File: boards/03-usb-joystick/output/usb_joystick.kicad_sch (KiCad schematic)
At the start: 19 parts, among them J1 TYPE-C, J2 Joystick, SW1 Button, SW2 Button, SW3 Button, SW4 Button, U1 MCU, Y1 16MHz

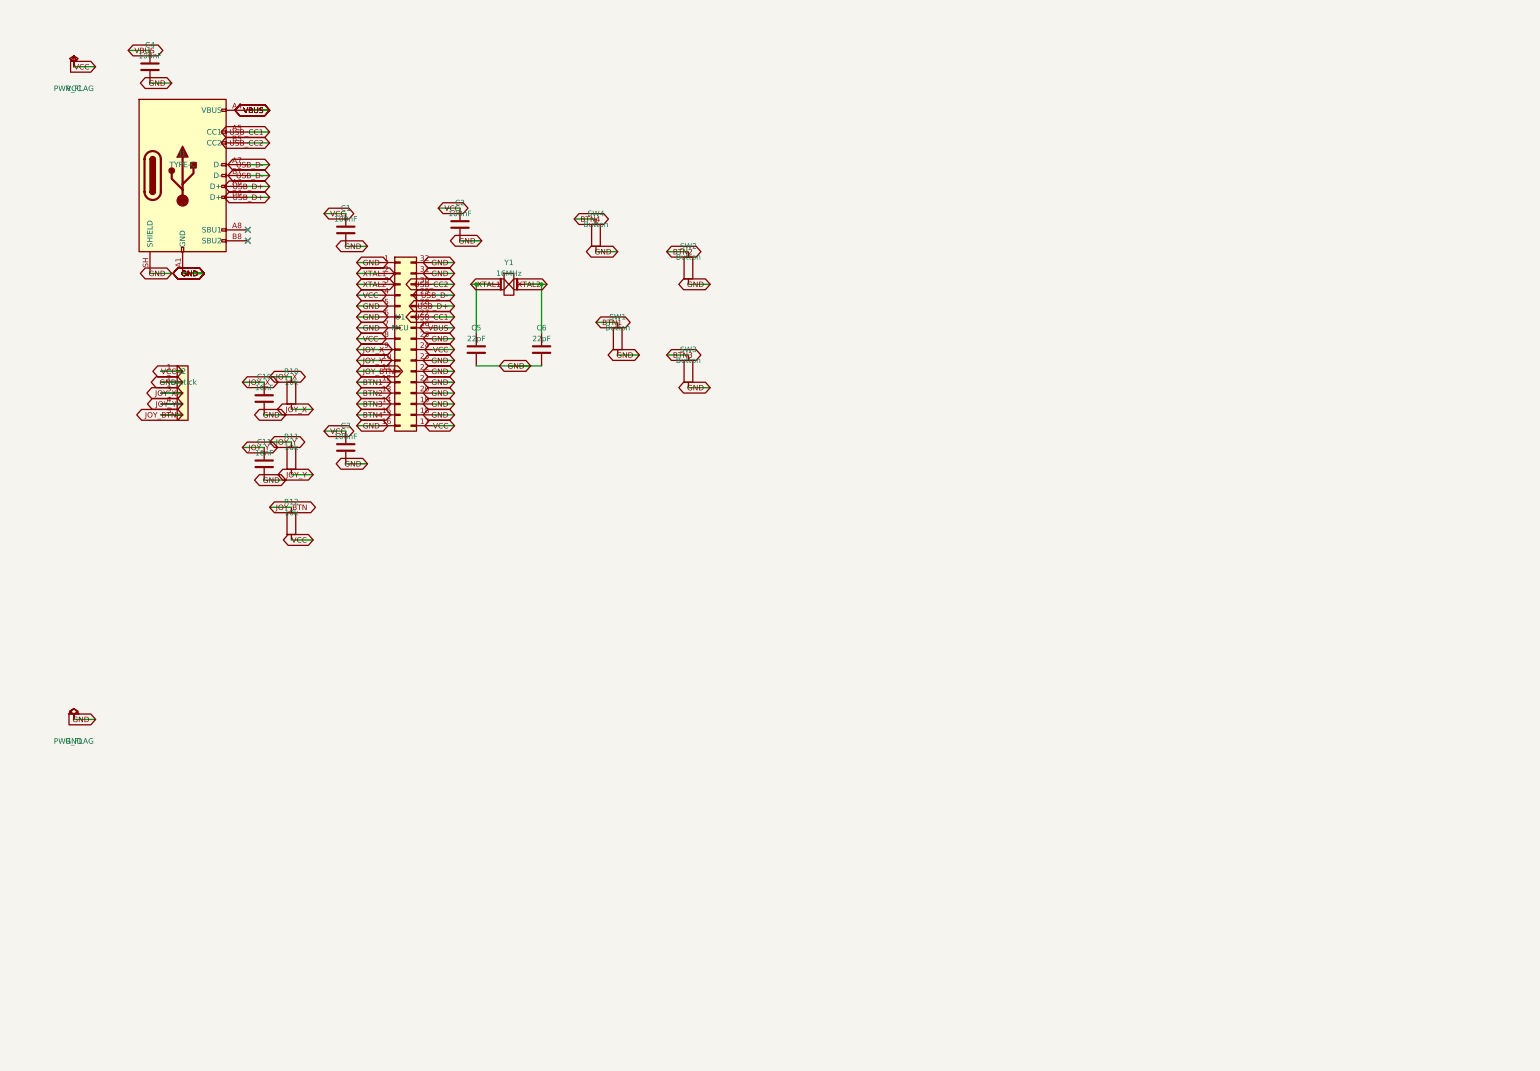
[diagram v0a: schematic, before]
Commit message: feat: prepare real demo boards and verified gallery releases
Redesign the controller, LVDS and SDRAM demos around real components and
ship checked assembly packages for boards 00-07, including firmware,
procurement reviews and hash-bound manufacturing evidence.

Add readiness reporting and gallery gates, scoped Cloudflare account
validation, and the routing, geometry, fabrication-rule, cache, LVS and
stripline fixes surfaced during the manufacturing audit.

Scaffold precision acquisition demo 08 and develop the real USB-C PD
power demo 09 with circuit checks, telemetry tests and saved routing
investigations. Keep incomplete examples explicitly blocked.

Preserve exact board bytes in Git and include hash-bound release renders.
Freeze the historical 32-pad joystick router fixture separately from the
real 44-pin design (Refs #5042).

Retire legacy manufacturing error allowances, point release-gate tests at
the real outputs, and run board04's scoped paid-drill validator in CI.
Keep original silkscreen defects as historical detector witnesses.
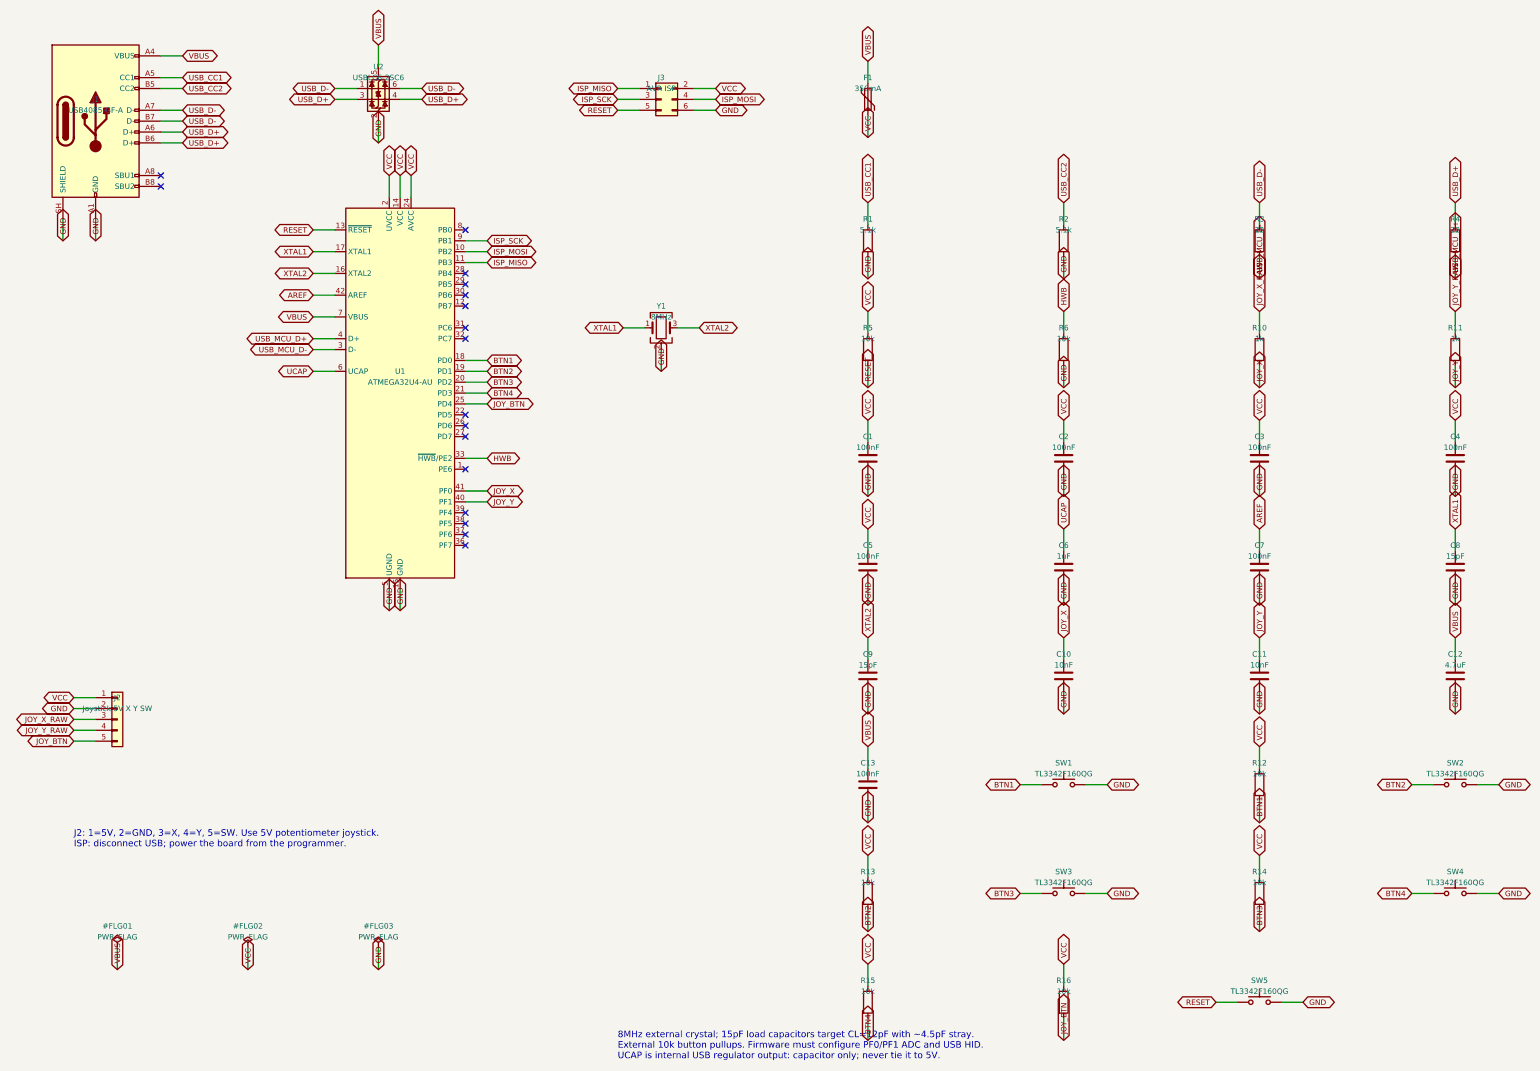
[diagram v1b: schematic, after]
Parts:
- removed SW1, SW2, SW3, SW4: Button, Button_Switch_SMD:SW_SPST_TL3342, symbol Device:R
- removed U1: MCU, Package_QFP:TQFP-32_7x7mm_P0.8mm, symbol Connector_Generic:Conn_02x16_Counter_Clockwise
- removed Y1: 16MHz, Crystal:Crystal_HC49-U_Vertical, symbol Device:Crystal
- added C12: 4.7uF, Capacitor_SMD:C_0603_1608Metric, symbol Device:C
- added C13, C7: 100nF, Capacitor_SMD:C_0603_1608Metric, symbol Device:C
- added C8, C9: 15pF, Capacitor_SMD:C_0603_1608Metric, symbol Device:C
- added F1: 350mA, Fuse:Fuse_1206_3216Metric, symbol Device:Polyfuse
- added J3: AVR ISP, Joystick:Samtec_TSM-103-01-T-DV, symbol Connector_Generic:Conn_02x03_Odd_Even
- added R1, R2: 5.1k, Resistor_SMD:R_0603_1608Metric, symbol Device:R
- added R13, R14, R15, R16, R5, R6: 10k, Resistor_SMD:R_0603_1608Metric, symbol Device:R
- added R3, R4: 22, Resistor_SMD:R_0402_1005Metric, symbol Device:R
- added SW1, SW2, SW3, SW4, SW5: TL3342F160QG, Button_Switch_SMD:SW_SPST_TL3342, symbol Switch:SW_Push
- added U1: ATMEGA32U4-AU, Package_QFP:TQFP-44_10x10mm_P0.8mm, symbol MCU_Microchip_ATmega:ATmega32U4-A
- added U2: USBLC6-2SC6, Package_TO_SOT_SMD:SOT-23-6, symbol Power_Protection:USBLC6-2SC6
- added Y1: 8MHz, Crystal:Crystal_SMD_3225-4Pin_3.2x2.5mm, symbol Device:Crystal_GND24
- C1, C2, C3, C4: footprint Capacitor_SMD:C_0402_1005Metric -> Capacitor_SMD:C_0603_1608Metric; LCSC (none) -> C45000; MPN (none) -> GRM188R71C104KA01D; Manufacturer (none) -> Murata
- C10, C11: value 16nF -> 10nF; footprint Capacitor_SMD:C_0402_1005Metric -> Capacitor_SMD:C_0603_1608Metric; LCSC (none) -> C77053; MPN (none) -> GRM188R71H103KA01D; Manufacturer (none) -> Murata
- C5: value 22pF -> 100nF; footprint Capacitor_SMD:C_0402_1005Metric -> Capacitor_SMD:C_0603_1608Metric; LCSC (none) -> C45000; MPN (none) -> GRM188R71C104KA01D; Manufacturer (none) -> Murata
- C6: value 22pF -> 1uF; footprint Capacitor_SMD:C_0402_1005Metric -> Capacitor_SMD:C_0603_1608Metric; LCSC (none) -> C97888; MPN (none) -> GRM188R71A105KA61D; Manufacturer (none) -> Murata
- J1: value TYPE-C -> USB4085-GF-A; footprint Connector_USB:USB_C_Receptacle_GCT_USB4105 -> Connector_USB:USB_C_Receptacle_GCT_USB4085; LCSC (none) -> C7095263; MPN (none) -> USB4085-GF-A; Manufacturer (none) -> GCT
- J2: value Joystick -> Joystick 5V X Y SW; footprint Module:Joystick_Analog -> Connector_JST:JST_PH_S5B-PH-SM4-TB_1x05-1MP_P2.00mm_Horizontal; LCSC (none) -> C265104; MPN (none) -> S5B-PH-SM4-TB(LF)(SN); Manufacturer (none) -> JST
- R10, R11: value 10k -> 1k; footprint Resistor_SMD:R_0402_1005Metric -> Resistor_SMD:R_0603_1608Metric; LCSC (none) -> C22548; MPN (none) -> RC0603FR-071KL; Manufacturer (none) -> Yageo
- R12: footprint Resistor_SMD:R_0402_1005Metric -> Resistor_SMD:R_0603_1608Metric; LCSC (none) -> C98220; MPN (none) -> RC0603FR-0710KL; Manufacturer (none) -> Yageo
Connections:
- net BTN1: now also R12.2, SW1.1, U1.18 (PD0)
- net BTN2: now also R13.2, SW2.1, U1.19 (PD1)
- net BTN3: now also R14.2, SW3.1, U1.20 (PD2)
- net BTN4: now also R15.2, SW4.1, U1.21 (PD3)
- net GND: now also C12.2, C13.2, C7.2, C8.2, C9.2, J3.6 (Pin_6), R1.2, R2.2, R6.2, SW1.2, SW2.2, SW3.2, SW4.2, SW5.2, U1.15 (GND), U1.23 (GND), U1.35 (GND), U1.43 (GND), U1.5 (UGND), U2.2 (GND), Y1.2 (G), Y1.4 (G)
- net JOY_BTN: now also R16.2, U1.25 (PD4); no longer R12.1
- net JOY_X: now also U1.41 (PF0); no longer J2.3 (Pin_3), R10.1
- net JOY_Y: now also U1.40 (PF1); no longer J2.4 (Pin_4), R11.1
- net USB_CC1: now also R1.1
- net USB_CC2: now also R2.1
- net USB_D+: now also R4.1, U2.3 (I/O2), U2.4 (I/O2)
- net USB_D-: now also R3.1, U2.1 (I/O1), U2.6 (I/O1)
- net VBUS: now also C12.1, C13.1, F1.1, U1.7 (VBUS), U2.5 (VBUS); no longer C4.1
- net VCC: now also C4.1, C5.1, R12.1, F1.2, J3.2 (Pin_2), R13.1, R14.1, R15.1, R16.1, R5.1, U1.14 (VCC), U1.2 (UVCC), U1.24 (AVCC), U1.34 (VCC), U1.44 (AVCC); no longer R12.2
- net XTAL1: now also C8.1, U1.17 (XTAL1), Y1.1; no longer C5.1
- net XTAL2: now also C9.1, U1.16 (XTAL2), Y1.3; no longer C6.1
- new net AREF: C7.1, U1.42 (AREF)
- new net HWB: R6.1, U1.33 (~{HWB}/PE2)
- new net ISP_MISO: J3.1 (Pin_1), U1.11 (PB3)
- new net ISP_MOSI: J3.4 (Pin_4), U1.10 (PB2)
- new net ISP_SCK: J3.3 (Pin_3), U1.9 (PB1)
- new net JOY_X_RAW: J2.3 (Pin_3), R10.1
- new net JOY_Y_RAW: J2.4 (Pin_4), R11.1
- new net RESET: J3.5 (Pin_5), R5.2, SW5.1, U1.13 (~{RESET})
- new net UCAP: C6.1, U1.6 (UCAP)
- new net USB_MCU_D+: R4.2, U1.4 (D+)
- new net USB_MCU_D-: R3.2, U1.3 (D-)
- no-connect marks 2 -> 17
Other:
- note added: "8MHz external crystal; 15pF load capacitors target CL=12pF with ~4.5pF stray. External 10k button pullups. Firmware must configure PF0/PF1 ADC and USB HID. UCAP is internal USB regulator output: capacitor only; never tie it to 5V."
- note added: "J2: 1=5V, 2=GND, 3=X, 4=Y, 5=SW. Use 5V potentiometer joystick. ISP: disconnect USB; power the board from the programmer."
- company: kicad-tools Demo -> kicad-tools
- title: USB Joystick Controller -> USB joystick controller — ATmega32U4
